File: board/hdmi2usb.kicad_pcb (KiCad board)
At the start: 8 copper layers, 185.4 x 108.6 mm, 446 parts, among them J1 USB_MICRO_B, J2 HDMI, J3 HDMI, J4 HDMI, J5 DVI-STACKED, J6 DVI-STACKED, J7 HDMI, J8 VHDCI, J9 DVI-STACKED, P1 CONN_7X2, P10 CONN_1, P11 CONN_1, P12 CONN_1, P13 CONN_1, P14 CONN_1, P15 CONN_1, P16 CONN_1, P17 CONN_1, P18 CONN_1, P19 CONN_1, P2 CONN_1, P20 CONN_1, P21 CONN_1, P22 CONN_1, P23 CONN_1, P24 CONN_1, P25 CONN_1, P26 CONN_1, P27 CONN_1, P28 CONN_1, P29 CONN_1, P3 CONN_1, P30 CONN_1, P31 CONN_1, P32 CONN_1, P33 CONN_1, P34 CONN_1, P35 CONN_1, P36 CONN_1, P37 CONN_1, P38 CONN_1, P39 CONN_1, P4 CONN_1, P40 CONN_1, P41 CONN_1, P42 CONN_1, P43 CONN_1, P44 CONN_1, P45 CONN_1, P46 CONN_1, P5 CONN_1, P6 CONN_1, P7 CONN_1, P8 CONN_1, P9 CONN_1, U1 CY7C68013A, U10 IP4776CZ38, U11 IP4776CZ38, U12 SPARTAN6LXXXX-CSG324, U13 FXO-HC536R, U2 M25P16, U3 LMR10530, U4 LMR10530, U5 LMR10530, U6 LP2997, U7 MT47H64M16HR, U8 IP4776CZ38, U9 IP4776CZ38, X1 CRYSTAL

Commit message: Issue #606 - Length Matching.
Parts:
- moved C10 117.5 mm to (51.8, 76.2)
- moved C12 117.5 mm to (43.7, 53.3)
- moved C14 117.5 mm to (97.5, 41.1)
- moved C16 117.5 mm to (124.0, 54.4)
- moved C23 117.5 mm to (107.2, 56.9)
- moved C24 117.5 mm to (116.8, 38.1)
- moved C3 117.5 mm to (38.6, 46.2)
- moved C4 117.5 mm to (48.8, 35.6)
- moved C48 117.5 mm to (105.2, 48.8)
- moved C5 117.5 mm to (37.1, 59.9)
- moved C54 117.5 mm to (122.9, 68.1)
- moved C66 117.5 mm to (149.9, 52.8)
- moved C9 117.5 mm to (47.2, 77.7)
- moved C93 117.5 mm to (147.8, 55.9)
- moved R100 117.5 mm to (165.6, 35.6)
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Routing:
- net N-00000430: track 39.9 -> 11.2 mm
- net /MT47H64M16HR/DDR-UDQS_N: track 9.91 -> 38.6 mm
- net /MT47H64M16HR/DDR-D10: track 10.8 -> 39.1 mm
- net /MT47H64M16HR/DDR-A0: track 18.5 -> 46.8 mm
- net /MT47H64M16HR/DDR-ODT: track 17.8 -> 45.9 mm
- net /MT47H64M16HR/DDR-D15: track 11.1 -> 39.2 mm
- net /MT47H64M16HR/DDR-D13: track 14.3 -> 42.0 mm
- net /MT47H64M16HR/DDR-D8: track 13.7 -> 40.2 mm
- net /MT47H64M16HR/DDR-CAS: track 13.2 -> 38.6 mm
- net /MT47H64M16HR/DDR-D9: track 12.1 -> 36.4 mm
- net /MT47H64M16HR/DDR-D4: track 17.9 -> 41.8 mm
- net /MT47H64M16HR/DDR-A2: track 24.6 -> 48.3 mm
- net /MT47H64M16HR/DDR-UDM: track 17.0 -> 40.4 mm
- net /MT47H64M16HR/DDR-UDQS_P: track 15.2 -> 38.5 mm
- net /MT47H64M16HR/DDR-CK_P: track 19.8 -> 42.8 mm
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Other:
- board size 185.4 x 108.6 mm -> 180.3 x 101 mm

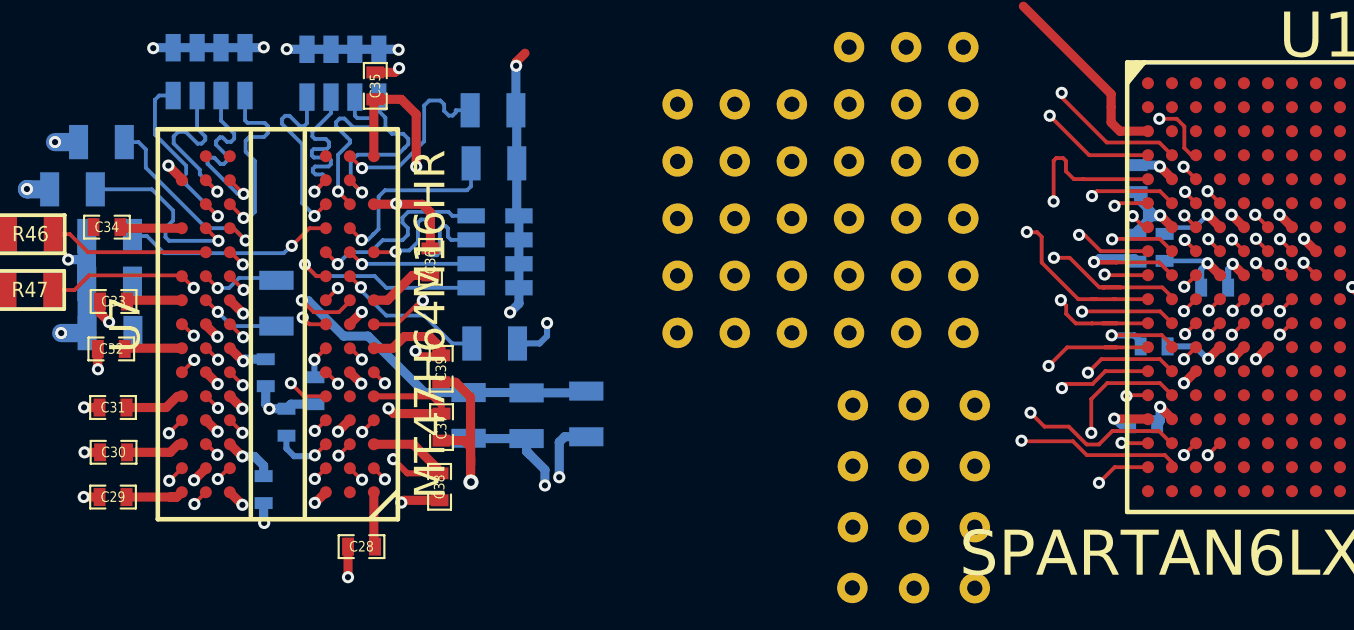
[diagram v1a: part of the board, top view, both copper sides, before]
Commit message: Issue #606 - Length Matching.
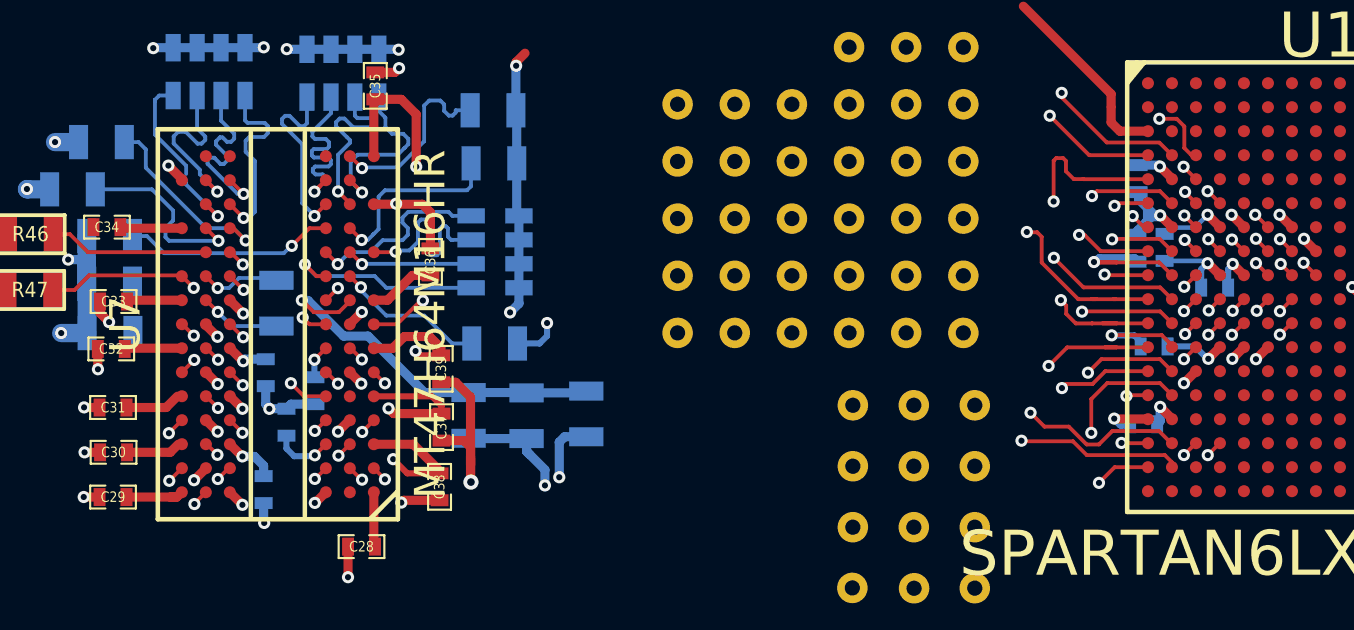
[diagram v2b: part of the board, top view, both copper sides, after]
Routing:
- net (no net): track 0.00 -> 102.4 mm, vias 0 -> 20
- net N-00000417: track 1.12 -> 62.3 mm
- net N-00000346: track 61.2 -> 0.00 mm
- net N-00000427: track 1.27 -> 61.8 mm
- net N-00000345: track 59.5 -> 0.00 mm
- net /hdmi/TMDS-RX1-1_N: track 106.7 -> 61.5 mm
- net GND: track 119.0 -> 83.5 mm, vias 90 -> 74
- net /hdmi/TMDS-RX1-2_N: track 64.8 -> 99.2 mm
- net N-00000431: track 34.5 -> 1.81 mm
- net N-00000285: track 3.41 -> 26.9 mm
- net /hdmi/P1-SCL: track 31.5 -> 7.94 mm
- net N-00000282: track 2.88 -> 25.4 mm
- net /hdmi/P1-HOT: track 30.1 -> 7.55 mm
- net N-00000423: track 21.3 -> 1.23 mm
- net /hdmi/TMDS-RX1-0_N: track 77.8 -> 97.8 mm
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
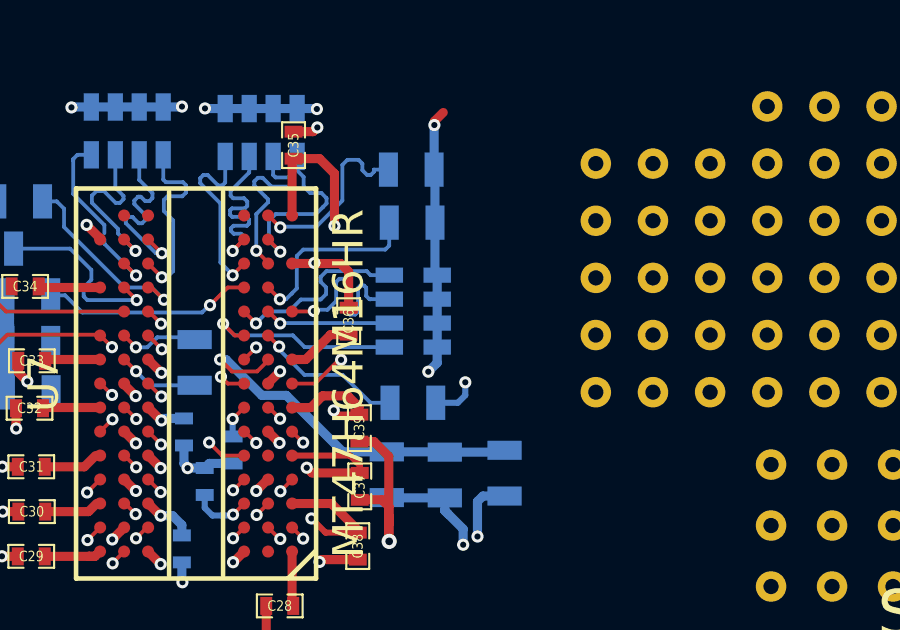
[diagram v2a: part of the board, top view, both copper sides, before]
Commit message: Issue #606 - Length Matching.
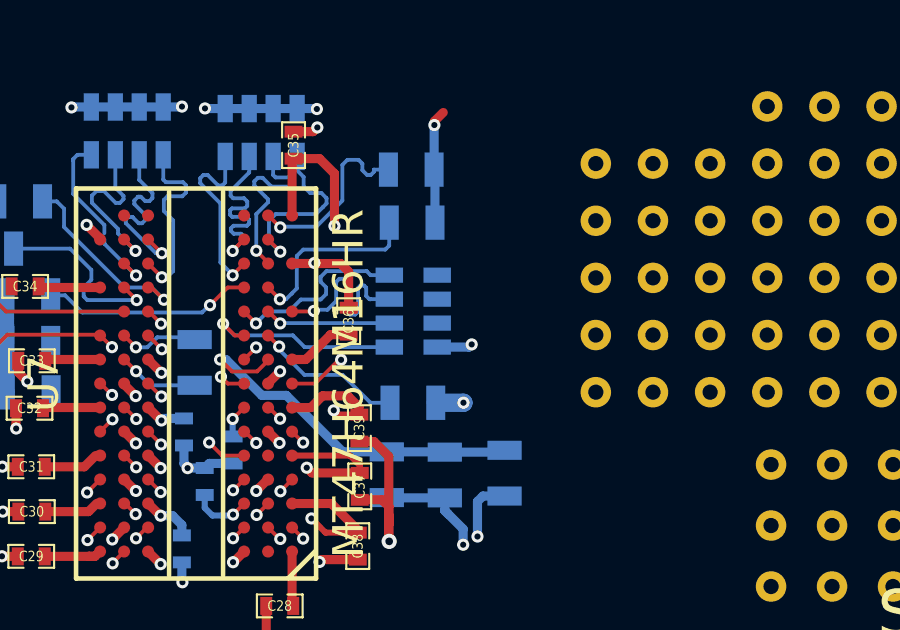
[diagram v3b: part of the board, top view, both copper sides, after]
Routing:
- net /hdmi/TMDS-RX1-1_N: track 61.5 -> 122.0 mm
- net N-00000427: track 61.8 -> 1.27 mm
- net N-00000285: track 26.9 -> 3.41 mm
- net /hdmi/P1-SCL: track 7.94 -> 31.5 mm
- net /hdmi/P1-HOT: track 7.55 -> 30.1 mm
- net N-00000282: track 25.4 -> 2.88 mm
- net /MT47H64M16HR/DDR-D0: track 35.2 -> 47.8 mm
- net /MT47H64M16HR/DDR-D1: track 30.1 -> 42.0 mm
- net DDR0V9: track 26.3 -> 22.4 mm
- net /MT47H64M16HR/DDR-D6: track 31.6 -> 27.9 mm
- net GND: track 83.5 -> 82.9 mm
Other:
- net class Default: clearance 0.1016 -> 0.09906
- rule trace_clearance: 0.1016 -> 0.09906

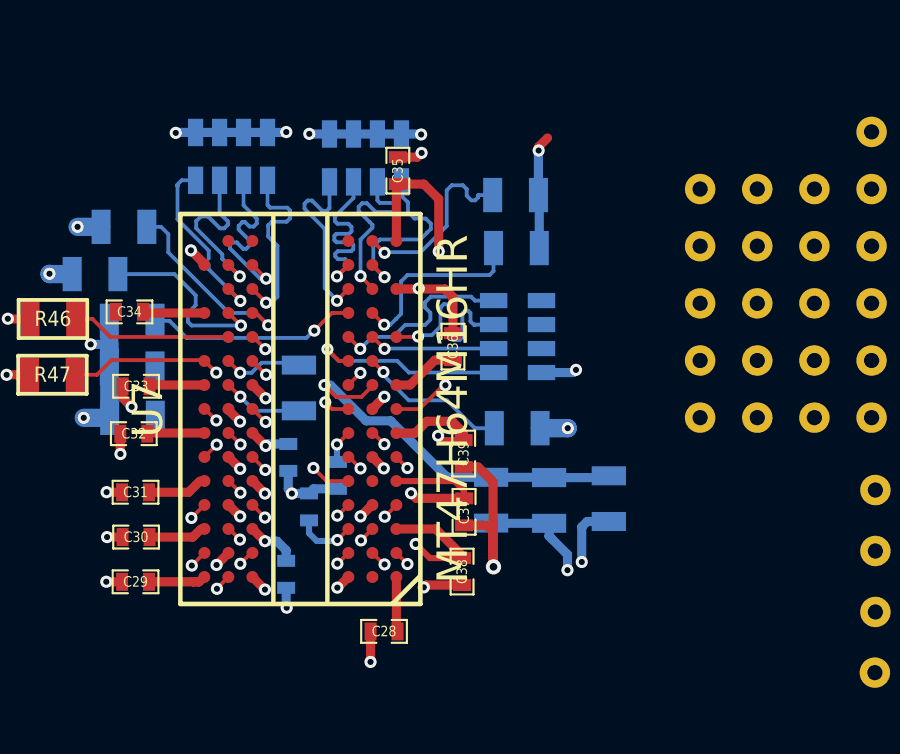
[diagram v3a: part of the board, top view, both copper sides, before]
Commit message: Issue #606 - Length Matching.
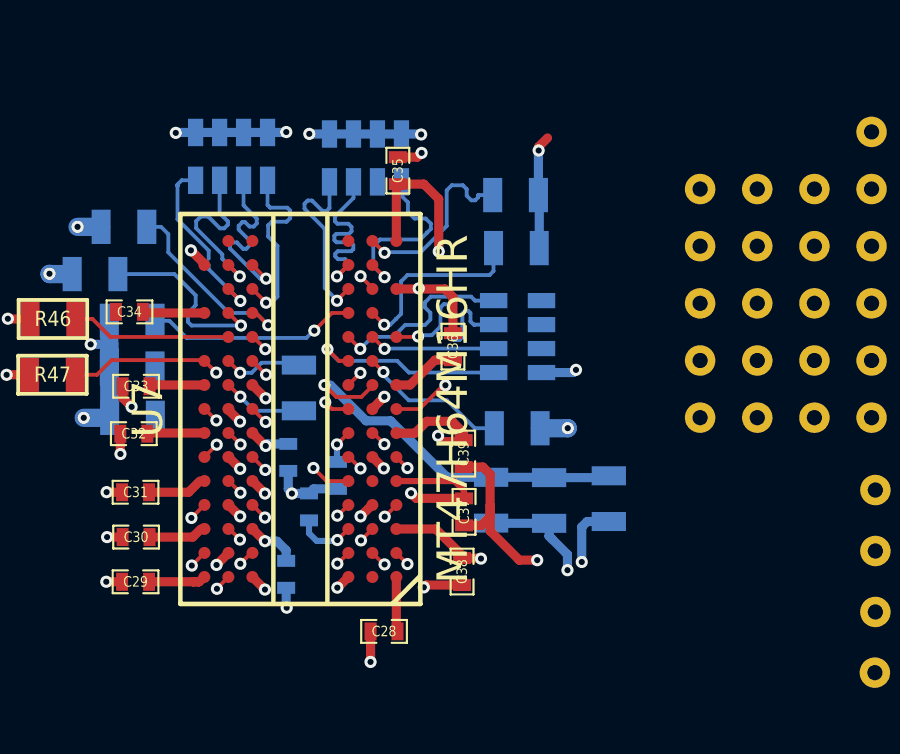
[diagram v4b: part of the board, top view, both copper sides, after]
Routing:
- net /MT47H64M16HR/DDR-D6: track 27.9 -> 41.8 mm
- net /MT47H64M16HR/DDR-D14: track 28.8 -> 42.1 mm
- net /MT47H64M16HR/DDR-D12: track 30.9 -> 41.9 mm
- net /MT47H64M16HR/DDR-LDM: track 32.1 -> 42.1 mm
- net /MT47H64M16HR/DDR-D0: track 47.8 -> 41.9 mm
- net /MT47H64M16HR/DDR-LDQS_N: track 36.2 -> 42.0 mm
- net /MT47H64M16HR/DDR-A3: track 49.1 -> 43.4 mm
- net /MT47H64M16HR/DDR-D11: track 36.5 -> 42.0 mm
- net /MT47H64M16HR/DDR-LDQS_P: track 36.9 -> 42.0 mm
- net /MT47H64M16HR/DDR-D9: track 36.4 -> 39.8 mm
- net /MT47H64M16HR/DDR-D10: track 39.1 -> 42.0 mm
- net /MT47H64M16HR/DDR-D8: track 40.2 -> 42.1 mm
- net /MT47H64M16HR/DDR-UDM: track 40.4 -> 42.0 mm
- net DDR1V8: track 55.9 -> 54.8 mm

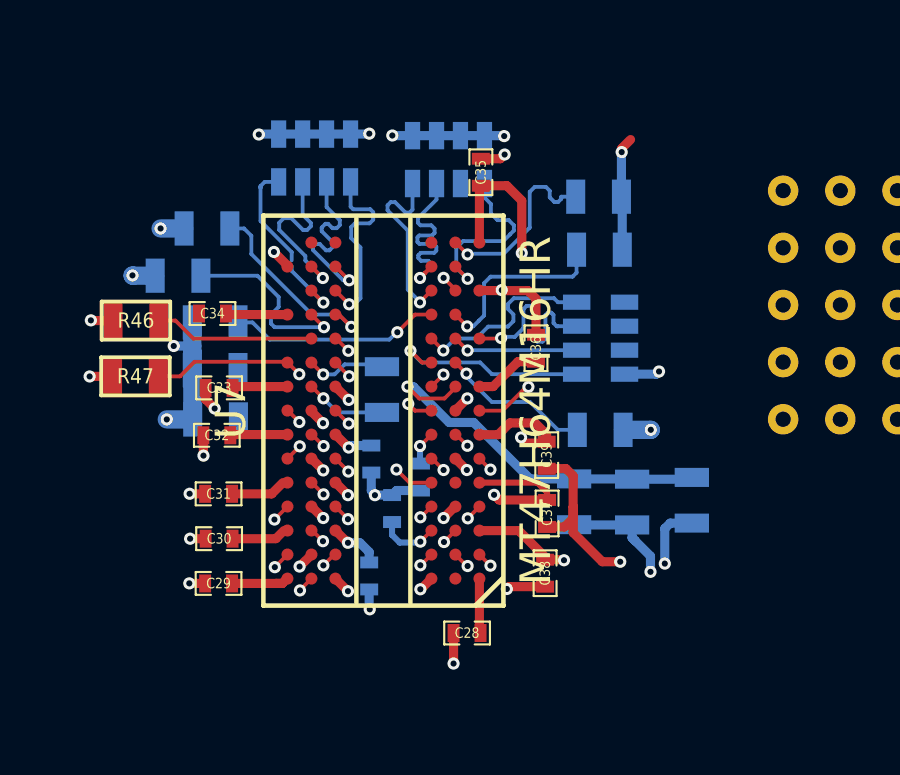
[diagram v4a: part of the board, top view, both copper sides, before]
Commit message: Issue #606 - Signal 1 is completed.
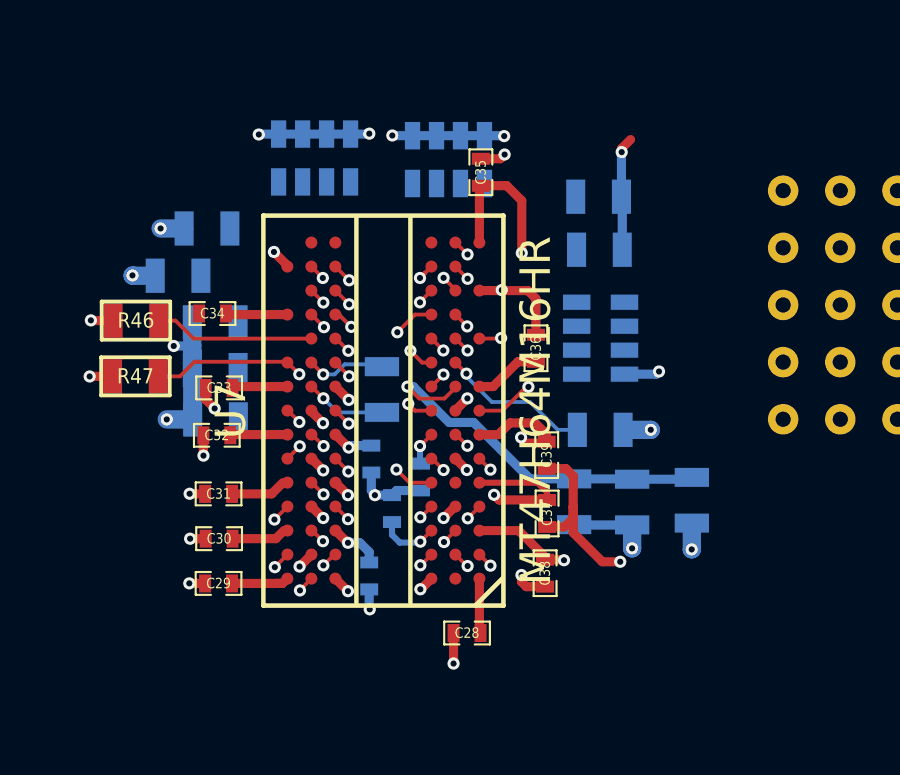
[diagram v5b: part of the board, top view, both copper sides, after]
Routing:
- net /MT47H64M16HR/DDR-A12: track 41.4 -> 34.9 mm
- net /MT47H64M16HR/DDR-A7: track 43.6 -> 37.7 mm
- net /MT47H64M16HR/DDR-WE: track 41.9 -> 36.1 mm
- net /MT47H64M16HR/DDR-A9: track 39.7 -> 33.9 mm
- net /MT47H64M16HR/DDR-BA1: track 36.0 -> 30.2 mm
- net /MT47H64M16HR/DDR-A10: track 37.9 -> 32.2 mm
- net /MT47H64M16HR/DDR-A11: track 43.4 -> 37.6 mm
- net /MT47H64M16HR/DDR-BA2: track 35.2 -> 29.5 mm
- net /MT47H64M16HR/DDR-A6: track 42.6 -> 36.9 mm
- net /MT47H64M16HR/DDR-A0: track 46.8 -> 41.1 mm
- net /MT47H64M16HR/DDR-A1: track 45.7 -> 40.0 mm
- net /MT47H64M16HR/DDR-A5: track 41.1 -> 35.5 mm
- net /MT47H64M16HR/DDR-A4: track 41.5 -> 36.2 mm
- net /MT47H64M16HR/DDR-A8: track 42.3 -> 37.2 mm
- net /MT47H64M16HR/DDR-A2: track 48.3 -> 43.4 mm
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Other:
- net class Default: clearance 0.09906 -> 0.1016
- rule trace_clearance: 0.09906 -> 0.1016

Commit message: Issue #606
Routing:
- net /MT47H64M16HR/DDR-BA2: track 29.5 -> 48.4 mm
- net /MT47H64M16HR/DDR-BA1: track 30.2 -> 48.4 mm
- net /MT47H64M16HR/DDR-A10: track 32.2 -> 48.4 mm
- net /MT47H64M16HR/DDR-BA0: track 30.2 -> 46.3 mm
- net /MT47H64M16HR/DDR-A9: track 33.9 -> 48.4 mm
- net /MT47H64M16HR/DDR-A12: track 34.9 -> 48.4 mm
- net /MT47H64M16HR/DDR-A5: track 35.5 -> 48.4 mm
- net /MT47H64M16HR/DDR-A4: track 36.2 -> 48.4 mm
- net /MT47H64M16HR/DDR-A6: track 36.9 -> 48.4 mm
- net /MT47H64M16HR/DDR-A8: track 37.2 -> 48.5 mm
- net /MT47H64M16HR/DDR-A11: track 37.6 -> 48.4 mm
- net /MT47H64M16HR/DDR-RAS: track 37.7 -> 48.4 mm
- net /MT47H64M16HR/DDR-A7: track 37.7 -> 48.4 mm
- net /MT47H64M16HR/DDR-CAS: track 38.6 -> 48.3 mm
- net /MT47H64M16HR/DDR-A1: track 40.0 -> 48.3 mm
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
